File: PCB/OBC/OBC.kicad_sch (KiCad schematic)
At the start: 5 parts, among them J1 Conn_02x24_Odd_Even

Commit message: Finishing schematics
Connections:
- net Can_H is gone; now on net GND: J1.23 (Pin_23)
- net Can_L is gone; now on net GND: J1.25 (Pin_25)
- net SPI_NSS is gone; now on net SPI_MOSI: J1.42 (Pin_42)
- net +Vbatt: no longer J1.2 (Pin_2)
- net ComsOBC_RX: now also J1.48 (Pin_48); no longer J1.47 (Pin_47)
- net EN_ADCS: now also J1.20 (Pin_20); no longer J1.19 (Pin_19)
- net EN_ADCS_5V: now also J1.21 (Pin_21); no longer J1.22 (Pin_22)
- net EN_COMS: now also J1.17 (Pin_17); no longer J1.18 (Pin_18)
- net EN_OBC: now also J1.34 (Pin_34); no longer J1.33 (Pin_33)
- net EN_PY1: now also J1.19 (Pin_19); no longer J1.20 (Pin_20)
- net EN_PY2: now also J1.15 (Pin_15); no longer J1.17 (Pin_17)
- net GND: now also J1.22 (Pin_22), J1.32 (Pin_32), J1.33 (Pin_33); no longer J1.14 (Pin_14), J1.21 (Pin_21), J1.24 (Pin_24), J1.26 (Pin_26), J1.31 (Pin_31), J1.34 (Pin_34), J1.40 (Pin_40)
- net I2C_SCL: now also J1.27 (Pin_27); no longer J1.28 (Pin_28)
- net I2C_SDA: now also J1.28 (Pin_28); no longer J1.27 (Pin_27)
- net Interrupción EPS: now also J1.31 (Pin_31); no longer J1.32 (Pin_32)
- net ObcComs_TX: now also J1.47 (Pin_47); no longer J1.48 (Pin_48)
- net PY2_RX: now also J1.38 (Pin_38); no longer J1.37 (Pin_37)
- net PY2_TX: now also J1.37 (Pin_37); no longer J1.38 (Pin_38)
- net SPI_MISO: now also J1.43 (Pin_43); no longer J1.44 (Pin_44)
- net SPI_MOSI: no longer J1.41 (Pin_41)
- net SPI_SCK: now also J1.44 (Pin_44); no longer J1.43 (Pin_43)
- net SW1: now also J1.14 (Pin_14); no longer J1.15 (Pin_15)
- new net CAN_H: J1.24 (Pin_24)
- new net CAN_L: J1.26 (Pin_26)
- new net CS_COMS: J1.41 (Pin_41)
- new net CS_PY2: J1.40 (Pin_40)
- new net EN_QUEMADOR: J1.18 (Pin_18)
- new net NR: J1.2 (Pin_2)
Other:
- moved on the sheet: J1

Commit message: PC104
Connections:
- net GND: now also J1.27 (Pin_27), J1.28 (Pin_28); no longer J1.29 (Pin_29), J1.30 (Pin_30)
- net I2C_SCL: now also J1.29 (Pin_29); no longer J1.27 (Pin_27)
- net I2C_SDA: now also J1.30 (Pin_30); no longer J1.28 (Pin_28)

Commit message: Coms memory finished
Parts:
- renumbered J1 to J2
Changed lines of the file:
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@@
 		(on_board yes)
 		(dnp no)
-		(property "Reference" "J1"
+		(property "Reference" "J2"
 			(at 240.538 66.294 0)
 			(effects
@@
 			(project "OBC"
 				(path "/e2c03eef-3b12-44a7-ba52-633d5337a24a"
-					(reference "J1")
+					(reference "J2")
 					(unit 1)
 				)

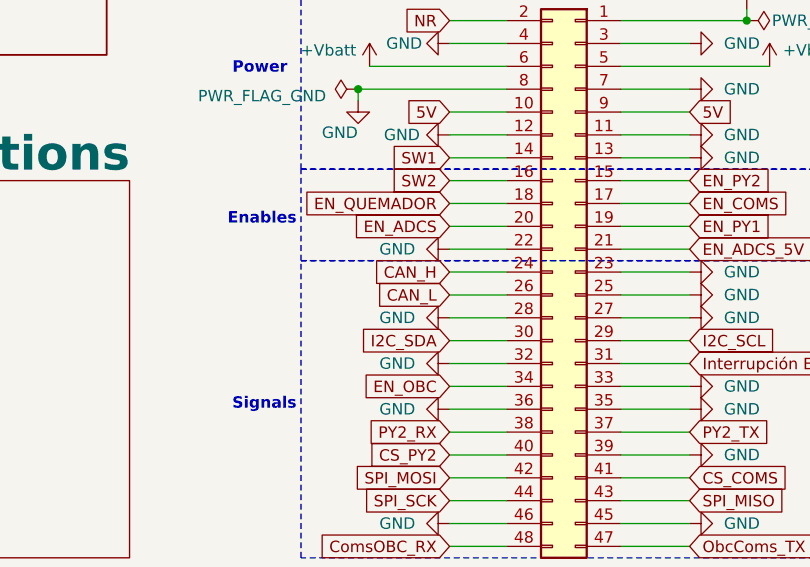
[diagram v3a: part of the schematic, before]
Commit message: Solo falta verificar el LDO
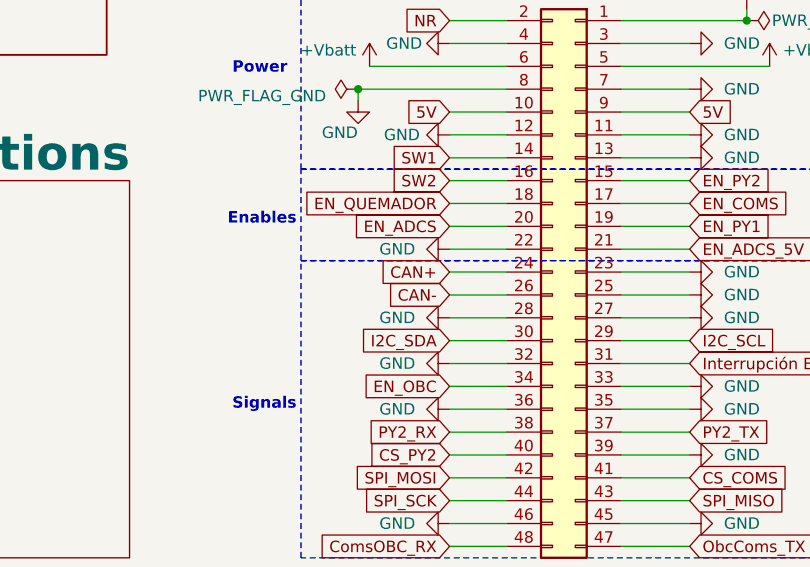
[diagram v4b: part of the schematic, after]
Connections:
- net CAN_H renamed CAN+
- net CAN_L renamed CAN-
